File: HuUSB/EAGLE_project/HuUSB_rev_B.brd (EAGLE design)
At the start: 65.4 x 55.2 mm, 21 parts, among them IC1 FT245RL-REEL, IC5 74HC245D,653, IC6 74HC245D,653, IC7 ATF22V10CQZ-20PU, J1 U-M-M5SS-W-2, J2 CONN_20X2NOSILK

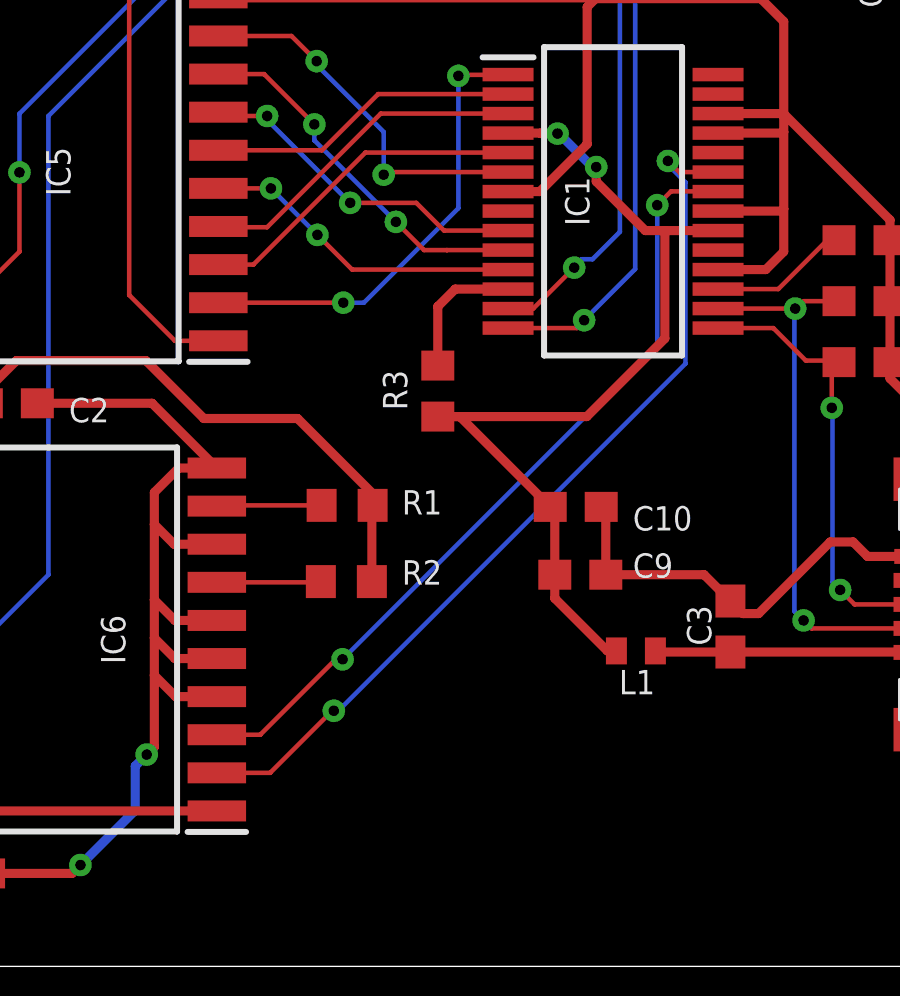
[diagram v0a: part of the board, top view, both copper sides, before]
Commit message: Add pull-up resistors to status bits coming from FT245RL
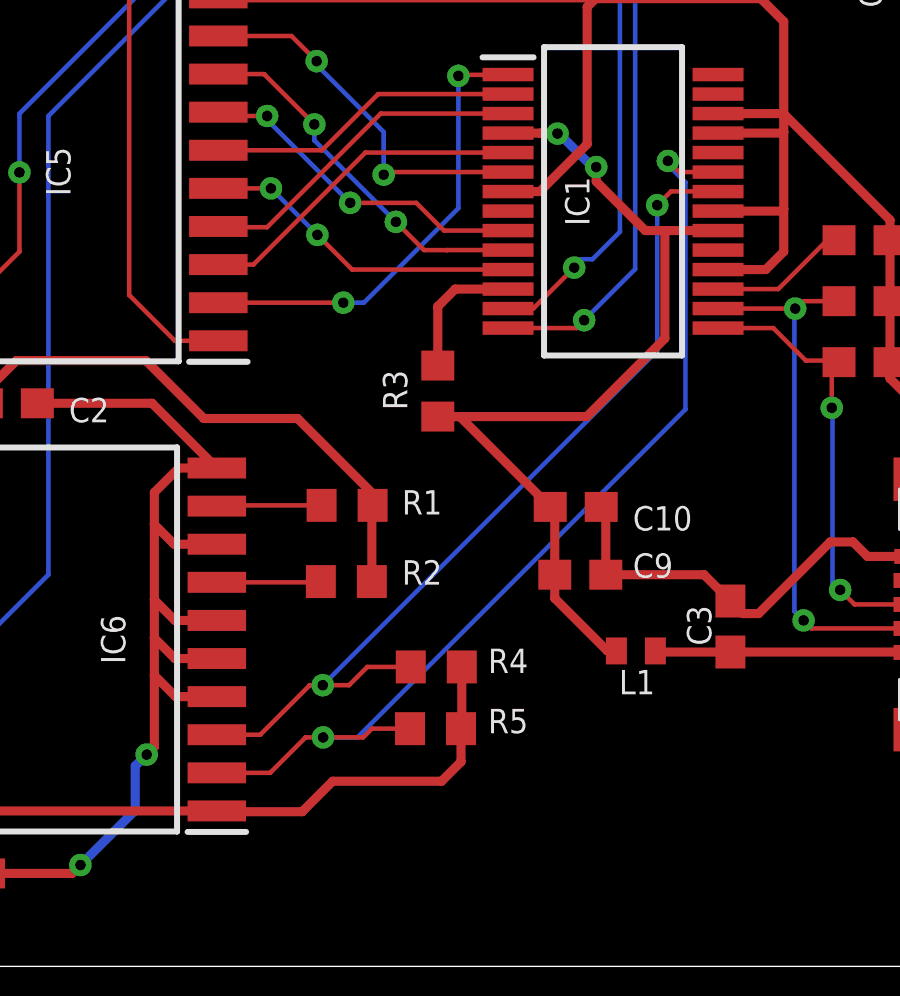
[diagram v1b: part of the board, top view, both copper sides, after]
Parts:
- added R4, R5: 47K, resistor:R0603
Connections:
- net +5V: now also R4.2, R5.2
- net N$45: now also R4.1
- net N$46: now also R5.1
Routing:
- net +5V: track 167.9 -> 179.9 mm
- net N$46: track 30.1 -> 34.0 mm
- net N$45: track 26.9 -> 30.2 mm
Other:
- board text added: "JLCJLCJLCJLC"
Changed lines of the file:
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@@
 <setting verticaltext="up"/>
 </settings>
-<grid distance="1" unitdist="mil" unit="mil" style="lines" multiple="1" display="yes" altdistance="5" altunitdist="mil" altunit="mil"/>
+<grid distance="5" unitdist="mil" unit="mil" style="lines" multiple="1" display="yes" altdistance="5" altunitdist="mil" altunit="mil"/>
 <layers>
 <layer number="1" name="Top" color="4" fill="1" visible="yes" active="yes"/>
@@
 <text x="7.62" y="52.07" size="1.016" layer="27" align="bottom-right">NC :40</text>
 <wire x1="0" y1="54.61" x2="0.635" y2="55.245" width="0" layer="20"/>
-<text x="37.465" y="5.207" size="1.778" layer="27">HuUSB, ver. B</text>
-<text x="37.465" y="2.5654" size="1.778" layer="27">(c) 2021, Dave Shadoff</text>
+<text x="38.8366" y="3.8862" size="1.778" layer="27">HuUSB, ver. B</text>
+<text x="38.862" y="1.6256" size="1.778" layer="27">(c) 2021, Dave Shadoff</text>
 <wire x1="58.0644" y1="48.0822" x2="58.0644" y2="45.5676" width="0.1524" layer="25"/>
+<text x="60.325" y="2.921" size="0.8128" layer="28" rot="MR0">JLCJLCJLCJLC</text>
 </plain>
 <attributes>
@@
 <attribute name="NAME" x="58.0136" y="33.3248" size="0.8128" layer="25" rot="R270"/>
 </element>
+<element name="R4" library="resistor" library_urn="urn:adsk.eagle:library:348" package="R0603" package3d_urn="urn:adsk.eagle:package:23555/3" value="47K" x="41.148" y="9.9822" smashed="yes">
+<attribute name="NAME" x="42.8752" y="9.779" size="0.8128" layer="25"/>
+</element>
+<element name="R5" library="resistor" library_urn="urn:adsk.eagle:library:348" package="R0603" package3d_urn="urn:adsk.eagle:package:23555/3" value="47K" x="41.1226" y="7.9248" smashed="yes">
+<attribute name="NAME" x="42.8752" y="7.7724" size="0.8128" layer="25"/>
+</element>
 </elements>
 <signals>
@@
 <wire x1="58.293" y1="35.9274" x2="55.626" y2="35.9274" width="0.3048" layer="1"/>
 <wire x1="55.626" y1="35.9274" x2="55.5752" y2="35.9782" width="0.3048" layer="1"/>
+<contactref element="R4" pad="2"/>
+<contactref element="R5" pad="2"/>
+<wire x1="41.998" y1="9.9822" x2="41.998" y2="7.9502" width="0.3048" layer="1"/>
+<wire x1="41.998" y1="7.9502" x2="41.9726" y2="7.9248" width="0.3048" layer="1"/>
+<wire x1="41.9726" y1="7.9248" x2="41.9726" y2="6.819" width="0.3048" layer="1"/>
+<wire x1="37.6936" y1="6.1722" x2="36.6776" y2="5.1562" width="0.3048" layer="1"/>
+<wire x1="36.6776" y1="5.1562" x2="33.8588" y2="5.1562" width="0.3048" layer="1"/>
+<wire x1="33.8588" y1="5.1562" x2="33.8334" y2="5.1816" width="0.3048" layer="1"/>
+<wire x1="41.9726" y1="6.819" x2="41.3258" y2="6.1722" width="0.3048" layer="1"/>
+<wire x1="41.3258" y1="6.1722" x2="37.6936" y2="6.1722" width="0.3048" layer="1"/>
 </signal>
 <signal name="N$28">
@@
 <wire x1="48.9728" y1="25.8334" x2="48.514" y2="25.3746" width="0.1524" layer="1"/>
 <via x="48.514" y="25.3746" extent="1-16" drill="0.35"/>
-<wire x1="48.514" y1="25.3746" x2="48.514" y2="20.7264" width="0.1524" layer="16"/>
-<via x="38.0238" y="10.2362" extent="1-16" drill="0.35"/>
-<wire x1="38.0238" y1="10.2362" x2="37.7952" y2="10.2362" width="0.1524" layer="1"/>
+<wire x1="48.514" y1="25.3746" x2="48.514" y2="20.5232" width="0.1524" layer="16"/>
+<via x="37.3634" y="9.3726" extent="1-16" drill="0.35"/>
+<wire x1="37.3634" y1="9.3726" x2="36.9316" y2="9.3726" width="0.1524" layer="1"/>
 <wire x1="35.2806" y1="7.7216" x2="33.8334" y2="7.7216" width="0.1524" layer="1"/>
 <wire x1="50.5408" y1="25.8266" x2="50.534" y2="25.8334" width="0.1524" layer="1"/>
 <wire x1="50.534" y1="25.8334" x2="48.9728" y2="25.8334" width="0.1524" layer="1"/>
-<wire x1="48.514" y1="20.7264" x2="38.0238" y2="10.2362" width="0.1524" layer="16"/>
-<wire x1="37.7952" y1="10.2362" x2="35.2806" y2="7.7216" width="0.1524" layer="1"/>
+<wire x1="48.514" y1="20.5232" x2="37.3634" y2="9.3726" width="0.1524" layer="16"/>
+<wire x1="36.9316" y1="9.3726" x2="35.2806" y2="7.7216" width="0.1524" layer="1"/>
+<contactref element="R4" pad="1"/>
+<wire x1="40.298" y1="9.9822" x2="38.8502" y2="9.9822" width="0.1524" layer="1"/>
+<wire x1="38.8502" y1="9.9822" x2="38.2406" y2="9.3726" width="0.1524" layer="1"/>
+<wire x1="38.2406" y1="9.3726" x2="37.3634" y2="9.3726" width="0.1524" layer="1"/>
 </signal>
 <signal name="N$46">
@@
 <wire x1="49.4538" y1="26.1366" x2="48.8696" y2="26.7208" width="0.1524" layer="16"/>
 <wire x1="48.8696" y1="26.8478" x2="48.8696" y2="26.7208" width="0.1524" layer="16"/>
-<wire x1="49.4538" y1="26.1366" x2="49.4538" y2="20.0914" width="0.1524" layer="16"/>
-<wire x1="49.4538" y1="20.0914" x2="37.8841" y2="8.5217" width="0.1524" layer="16"/>
-<wire x1="37.7317" y1="8.5217" x2="37.8841" y2="8.5217" width="0.1524" layer="16"/>
-<via x="37.7317" y="8.5217" extent="1-16" drill="0.35"/>
-<wire x1="37.7317" y1="8.5217" x2="37.6809" y2="8.5217" width="0.1524" layer="1"/>
+<wire x1="49.4538" y1="26.1366" x2="49.4538" y2="18.5674" width="0.1524" layer="16"/>
+<wire x1="49.4538" y1="18.5674" x2="38.5191" y2="7.6327" width="0.1524" layer="16"/>
+<wire x1="37.3761" y1="7.6327" x2="38.5191" y2="7.6327" width="0.1524" layer="16"/>
+<via x="37.3761" y="7.6327" extent="1-16" drill="0.35"/>
+<wire x1="37.3761" y1="7.6327" x2="36.7919" y2="7.6327" width="0.1524" layer="1"/>
 <wire x1="35.6108" y1="6.4516" x2="33.8334" y2="6.4516" width="0.1524" layer="1"/>
-<wire x1="37.6809" y1="8.5217" x2="35.6108" y2="6.4516" width="0.1524" layer="1"/>
+<wire x1="36.7919" y1="7.6327" x2="35.6108" y2="6.4516" width="0.1524" layer="1"/>
+<contactref element="R5" pad="1"/>
+<wire x1="40.2726" y1="7.9248" x2="39.0026" y2="7.9248" width="0.1524" layer="1"/>
+<wire x1="39.0026" y1="7.9248" x2="38.7105" y2="7.6327" width="0.1524" layer="1"/>
+<wire x1="38.7105" y1="7.6327" x2="37.3761" y2="7.6327" width="0.1524" layer="1"/>
 </signal>
 </signals>
